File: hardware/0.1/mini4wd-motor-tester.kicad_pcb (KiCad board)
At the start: 2 copper layers, 108 x 48 mm, 104 parts, among them J1 USB_C_Receptacle_USB2.0_16P, J2 JST SH, J3 JST SH, J4 JST XH, M1 Motor_DC, Q2 AO3401A, Q3 2N7002, SW1 RA, SW2 RA, SW3 EC11, U1 TLV62130, U10 GP2S700HCP, U2 USBLC6-2SC6, U3 RT9080-33GJ5, U4 MCP4725, U5 ESP32-S3-WROOM-1, U6 INA219AxDCN, U7 DRV8837, U8 GP2S700HCP, U9 TMP1075DSG

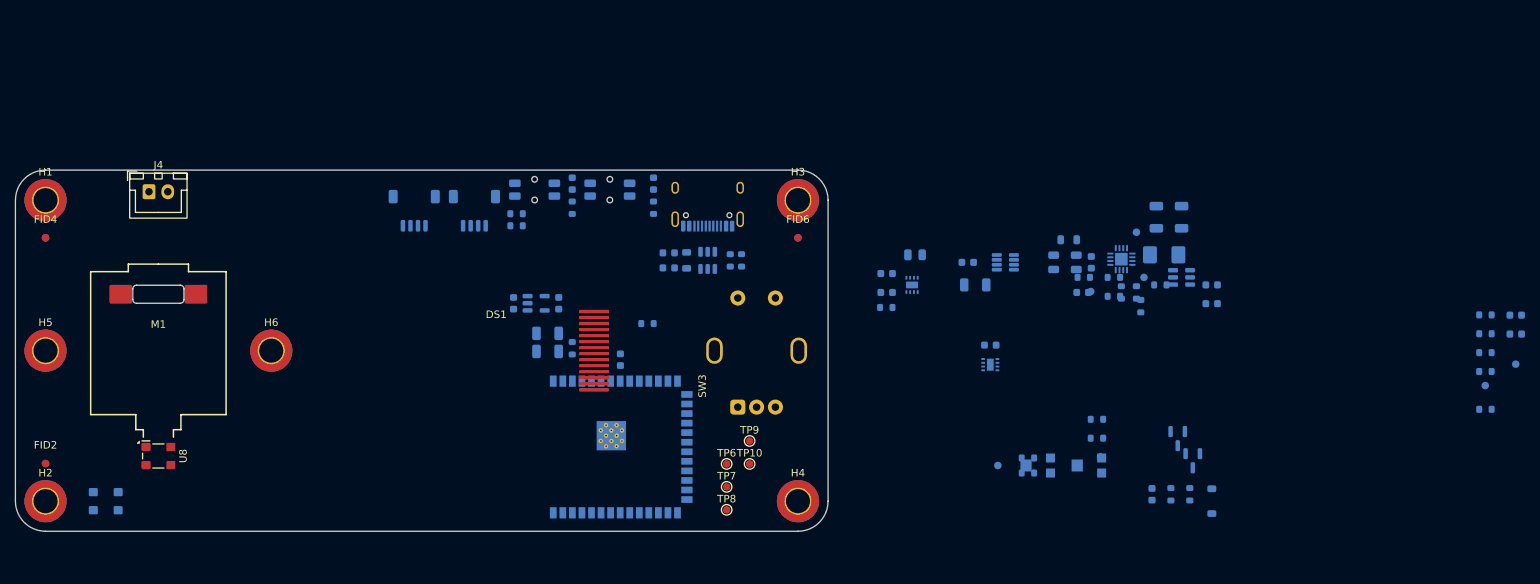
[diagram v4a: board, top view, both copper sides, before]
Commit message: rough placement of all parts on smaller board
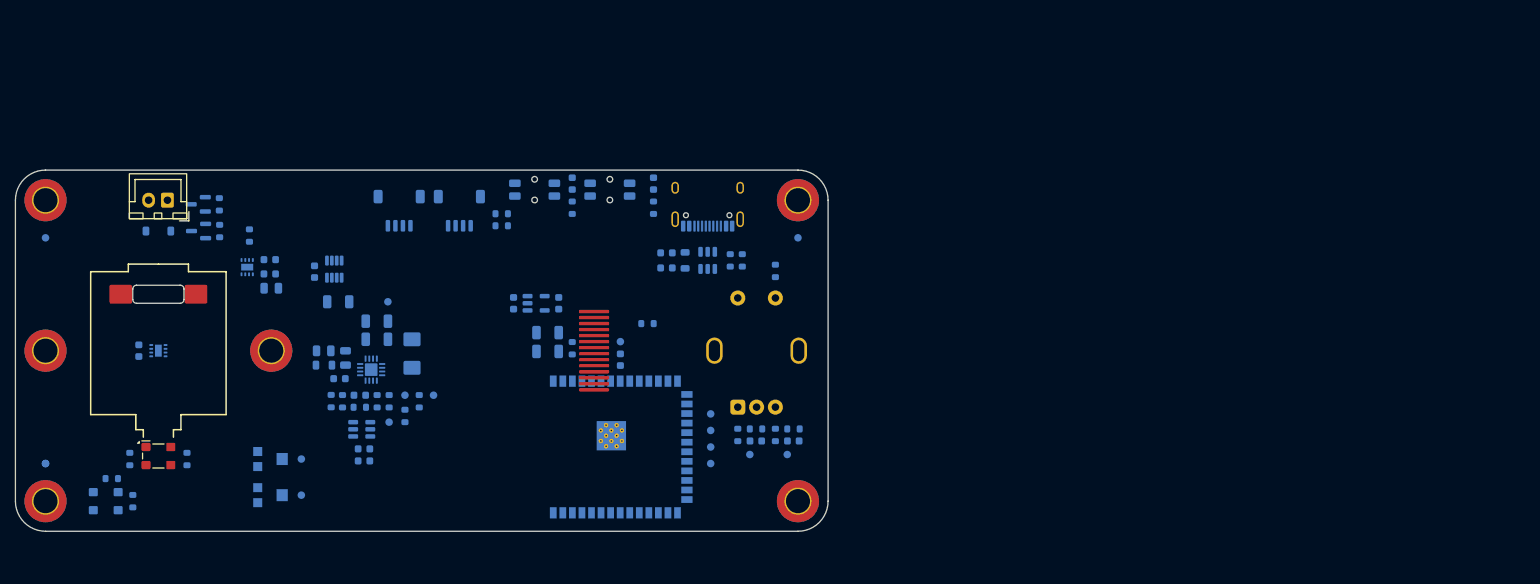
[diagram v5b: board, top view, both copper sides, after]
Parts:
- removed C24: 100n, Capacitor_SMD:C_0603_1608Metric
- removed FID4, FID6: Fiducial, Fiducial:Fiducial_1mm_Mask3mm
- added TP13: TP, TestPoint:TestPoint_Pad_D1.0mm, B.Cu at (121.6, 105.9)
- C12: value 100n -> 1u
- FID2, TP10, TP6, TP7, TP8, TP9: moved to B.Cu
- moved D3 144.5 mm to (85.0, 84.1), turned to 180 degrees
- moved Q2 135.6 mm to (90.3, 84.1), turned to 180 degrees
- moved Q3 133.8 mm to (90.3, 80.5), turned to 180 degrees
- moved R28 133.6 mm to (93.1, 84.1)
- moved R27 132.2 mm to (93.1, 80.5)
- moved R25 131.2 mm to (78.8, 117.0)
- moved R26 128.4 mm to (81.6, 120.0), turned to -90 degrees
- moved R22 119.4 mm to (81.2, 114.4), turned to -90 degrees
- moved C11 114.7 mm to (112.3, 113.0), turned to 180 degrees
- moved C12 114.6 mm to (112.3, 114.7)
- moved C22 113.2 mm to (82.4, 100.0), turned to 90 degrees
- moved R17 111.8 mm to (88.8, 114.4), turned to -90 degrees
- moved U4 110.8 mm to (112.0, 110.5), turned to 180 degrees
- moved U9 110.6 mm to (85.0, 100.0)
- moved RV2 108.6 mm to (100.0, 119.2), turned to 0 degrees
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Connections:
- C12 pad 1: +3V3 -> GND
- C12 pad 2: GND -> +3V3
- R6 pad 1: +VMOT -> +3V3

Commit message: I think the final form has been reached?
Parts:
- removed FID5: Fiducial, Fiducial:Fiducial_1mm_Mask3mm
- added G1: ~, josh-logos:josh-details, B.Cu at (103.0, 82.2)
- added kibuzzard-697A0689: G***, kibuzzard-697A0689, F.Cu at (125.0, 121.0)
- moved FID2 30.0 mm to (70.0, 85.0)
- moved R28 17.0 mm to (76.2, 84.1), turned to 90 degrees
- moved Q3 14.9 mm to (77.3, 87.8)
- moved R27 14.9 mm to (80.1, 87.8)
- moved Q2 11.4 mm to (79.0, 84.1), turned to 0 degrees
- moved H3 8.00 mm to (162.0, 80.0)
- moved H4 8.00 mm to (162.0, 120.0)
- moved FID1 7.99 mm to (162.0, 85.0)
- moved U5 7.65 mm to (135.1, 111.9)
- moved R24 7.65 mm to (142.4, 95.5)
- moved TP10 7.60 mm to (150.8, 108.4)
- moved TP6 7.60 mm to (150.8, 110.6)
- moved TP7 7.60 mm to (150.8, 115.0)
- moved TP9 7.60 mm to (150.8, 112.8)
- moved SW3 7.50 mm to (154.5, 107.5)
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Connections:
- J4 pad 1: Net-(D3-K) -> GND
- J4 pad 2: GND -> Net-(D3-K)
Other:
- board size 108 x 48 mm -> 100 x 48 mm
- board text added: "+"
- board text added: "-"
- board text added: "BOOT"
- board text added: "I2C"
- board text added: "MINI4WD MOTOR TESTER REVISION 1.0"
- board text added: "PWR"
- board text added: "RESET"
- board text added: "STAT"
- board text added: "UART"

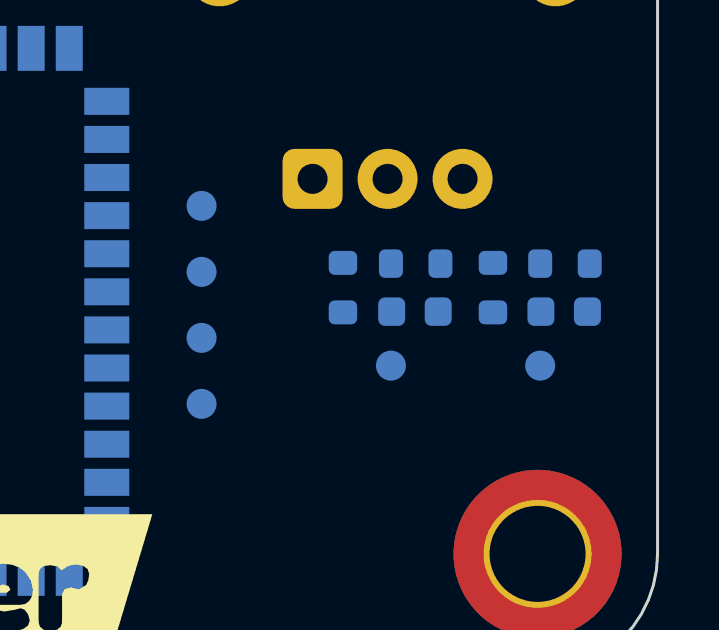
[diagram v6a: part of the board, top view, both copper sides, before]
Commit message: move encoder passives in from the edge
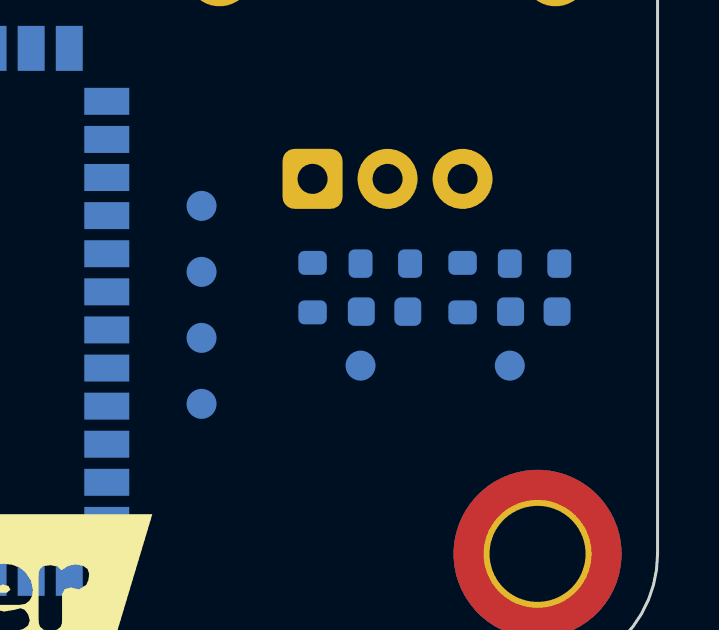
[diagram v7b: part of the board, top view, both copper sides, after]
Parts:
- moved TP4 1.01 mm to (156.1, 113.7)
- moved TP5 1.01 mm to (161.1, 113.7)
- moved C20 1.01 mm to (156.9, 111.9)
- moved C21 1.01 mm to (161.9, 111.9)
- moved R18 1.01 mm to (154.5, 111.1)
- moved R19 1.01 mm to (156.9, 110.3)
- moved R20 1.01 mm to (159.5, 111.1)
- moved R21 1.01 mm to (161.9, 110.3)
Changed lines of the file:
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@@
 	(footprint "Capacitor_SMD:C_0603_1608Metric"
 		(layer "B.Cu")
-		(at 162.8875 111.925)
+		(at 161.875 111.925)
 		(descr "Capacitor SMD 0603 (1608 Metric), square (rectangular) end terminal, IPC-7351 nominal, (Body size source: IPC-SM-782 page 76, https://www.pcb-3d.com/wordpress/wp-content/uploads/ipc-sm-782a_amendment_1_and_2.pdf), generated with kicad-footprint-generator")
 		(tags "capacitor")
@@
 	(footprint "Resistor_SMD:R_0603_1608Metric"
 		(layer "B.Cu")
-		(at 162.9125 110.325 180)
+		(at 161.9 110.325 180)
 		(descr "Resistor SMD 0603 (1608 Metric), square (rectangular) end terminal, IPC-7351 nominal, (Body size source: IPC-SM-782 page 72, https://www.pcb-3d.com/wordpress/wp-content/uploads/ipc-sm-782a_amendment_1_and_2.pdf), generated with kicad-footprint-generator")
 		(tags "resistor")
@@
 	(footprint "TestPoint:TestPoint_Pad_D1.0mm"
 		(layer "B.Cu")
-		(at 157.1125 113.725 180)
+		(at 156.1 113.725 180)
 		(descr "SMD pad as test Point, diameter 1.0mm")
 		(tags "test point SMD pad")
@@
 	(footprint "Resistor_SMD:R_0603_1608Metric"
 		(layer "B.Cu")
-		(at 155.5125 111.125 90)
+		(at 154.5 111.125 90)
 		(descr "Resistor SMD 0603 (1608 Metric), square (rectangular) end terminal, IPC-7351 nominal, (Body size source: IPC-SM-782 page 72, https://www.pcb-3d.com/wordpress/wp-content/uploads/ipc-sm-782a_amendment_1_and_2.pdf), generated with kicad-footprint-generator")
 		(tags "resistor")
@@
 	(footprint "Capacitor_SMD:C_0603_1608Metric"
 		(layer "B.Cu")
-		(at 157.9125 111.925)
+		(at 156.9 111.925)
 		(descr "Capacitor SMD 0603 (1608 Metric), square (rectangular) end terminal, IPC-7351 nominal, (Body size source: IPC-SM-782 page 76, https://www.pcb-3d.com/wordpress/wp-content/uploads/ipc-sm-782a_amendment_1_and_2.pdf), generated with kicad-footprint-generator")
 		(tags "capacitor")
@@
 	(footprint "Resistor_SMD:R_0603_1608Metric"
 		(layer "B.Cu")
-		(at 160.5125 111.125 90)
+		(at 159.5 111.125 90)
 		(descr "Resistor SMD 0603 (1608 Metric), square (rectangular) end terminal, IPC-7351 nominal, (Body size source: IPC-SM-782 page 72, https://www.pcb-3d.com/wordpress/wp-content/uploads/ipc-sm-782a_amendment_1_and_2.pdf), generated with kicad-footprint-generator")
 		(tags "resistor")
@@
 	(footprint "TestPoint:TestPoint_Pad_D1.0mm"
 		(layer "B.Cu")
-		(at 162.0875 113.725 180)
+		(at 161.075 113.725 180)
 		(descr "SMD pad as test Point, diameter 1.0mm")
 		(tags "test point SMD pad")
@@
 	(footprint "Resistor_SMD:R_0603_1608Metric"
 		(layer "B.Cu")
-		(at 157.9375 110.325 180)
+		(at 156.925 110.325 180)
 		(descr "Resistor SMD 0603 (1608 Metric), square (rectangular) end terminal, IPC-7351 nominal, (Body size source: IPC-SM-782 page 72, https://www.pcb-3d.com/wordpress/wp-content/uploads/ipc-sm-782a_amendment_1_and_2.pdf), generated with kicad-footprint-generator")
 		(tags "resistor")

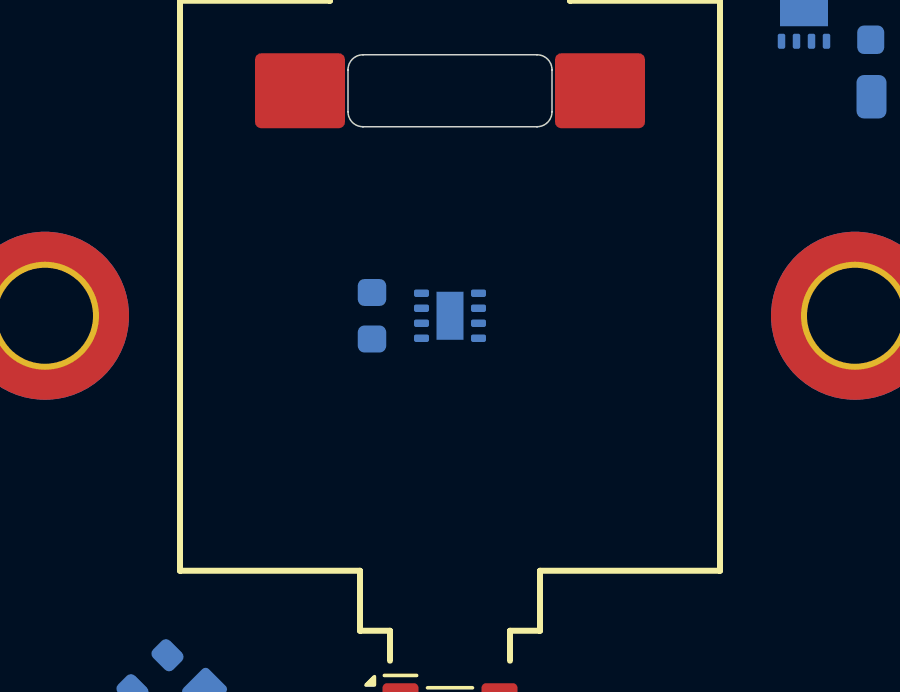
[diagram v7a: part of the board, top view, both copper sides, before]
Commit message: cutouts under the motor
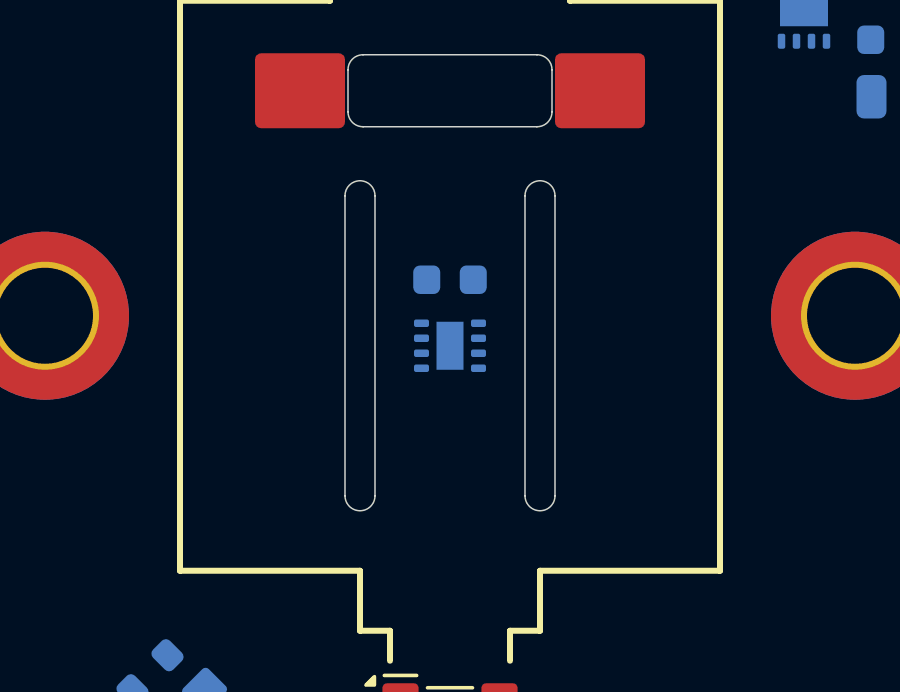
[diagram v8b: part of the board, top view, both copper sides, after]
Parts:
- moved C22 2.86 mm to (84.0, 98.8), turned to 180 degrees
- moved U9 1.00 mm to (84.0, 101.0)
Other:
- outline, holes or cut-outs redrawn
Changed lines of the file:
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@@
 		(tags "refective opto couple photo coupler")
 		(property "Reference" "U8"
-			(at 0 0 -0)
+			(at 0 0 0)
 			(layer "B.SilkS")
 			(effects
@@
 				(font
 					(size 0.001 0.001)
+					(thickness 0.15)
 				)
 			)
@@
 				(font
 					(size 0.001 0.001)
+					(thickness 0.15)
 				)
 			)
@@
 	(footprint "Package_SON:WSON-8-1EP_2x2mm_P0.5mm_EP0.9x1.6mm"
 		(layer "B.Cu")
-		(at 84 100 180)
+		(at 84 101 180)
 		(descr "8-Lead Plastic WSON, 2x2mm Body, 0.5mm Pitch, WSON-8, http://www.ti.com/lit/ds/symlink/lm27761.pdf")
 		(tags "WSON 8 1EP")
 		(property "Reference" "U9"
-			(at 0 2 0)
+			(at 0 -2.1 0)
 			(layer "B.SilkS")
 			(effects
@@
 	(footprint "Capacitor_SMD:C_0603_1608Metric"
 		(layer "B.Cu")
-		(at 81.4 100 90)
+		(at 84 98.8 180)
 		(descr "Capacitor SMD 0603 (1608 Metric), square (rectangular) end terminal, IPC-7351 nominal, (Body size source: IPC-SM-782 page 76, https://www.pcb-3d.com/wordpress/wp-content/uploads/ipc-sm-782a_amendment_1_and_2.pdf), generated with kicad-footprint-generator")
 		(tags "capacitor")
 		(property "Reference" "C22"
-			(at 0 1.43 90)
+			(at 0 1.43 0)
 			(layer "B.SilkS")
 			(hide yes)
@@
 		)
 		(property "Value" "100n"
-			(at 0 -1.43 90)
+			(at 0 -1.43 0)
 			(layer "B.Fab")
 			(effects
@@
 		)
 		(property "Datasheet" "~"
-			(at 0 0 90)
+			(at 0 0 0)
 			(layer "B.Fab")
 			(hide yes)
@@
 		)
 		(property "Description" ""
-			(at 0 0 90)
+			(at 0 0 0)
 			(layer "B.Fab")
 			(hide yes)
@@
 		)
 		(property "LCSC" "C14663"
-			(at 0 0 270)
+			(at 0 0 0)
 			(unlocked yes)
 			(layer "B.Fab")
@@
 		)
 		(property "Manufacturer" "Samsung Electro-Mechanics"
-			(at 0 0 270)
+			(at 0 0 0)
 			(unlocked yes)
 			(layer "B.Fab")
@@
 		)
 		(property "MPN " "CC0603KRX7R9BB104"
-			(at 0 0 270)
+			(at 0 0 0)
 			(unlocked yes)
 			(layer "B.Fab")
@@
 		)
 		(property "JLCSMT" ""
-			(at 0 0 90)
+			(at 0 0 180)
 			(unlocked yes)
 			(layer "B.Fab")
@@
 		(attr smd)
 		(fp_line
-			(start -0.14058 -0.51)
-			(end 0.14058 -0.51)
+			(start -0.14058 0.51)
+			(end 0.14058 0.51)
 			(stroke
 				(width 0.12)
@@
 		)
 		(fp_line
-			(start -0.14058 0.51)
-			(end 0.14058 0.51)
+			(start -0.14058 -0.51)
+			(end 0.14058 -0.51)
 			(stroke
 				(width 0.12)
@@
 		)
 		(fp_text user "${REFERENCE}"
-			(at 0 0 90)
+			(at 0 0 0)
 			(layer "B.Fab")
 			(effects
@@
 		)
 		(pad "1" smd roundrect
-			(at -0.775 0 90)
+			(at -0.775 0 180)
 			(size 0.9 0.95)
 			(layers "B.Cu" "B.Mask" "B.Paste")
@@
 		)
 		(pad "2" smd roundrect
-			(at 0.775 0 90)
+			(at 0.775 0 180)
 			(size 0.9 0.95)
 			(layers "B.Cu" "B.Mask" "B.Paste")
@@
 		)
 	)
+	(gr_rect
+		(start 78 94.5)
+		(end 90 107.5)
+		(stroke
+			(width 0.1)
+			(type solid)
+		)
+		(fill yes)
+		(layer "F.Mask")
+	)
+	(gr_arc
+		(start 80.5 96)
+		(mid 81 95.5)
+		(end 81.5 96)
+		(stroke
+			(width 0.05)
+			(type default)
+		)
+		(layer "Edge.Cuts")
+	)
 	(gr_line
 		(start 166 80)
@@
 	)
 	(gr_line
+		(start 81.5 96)
+		(end 81.5 106)
+		(stroke
+			(width 0.05)
+			(type default)
+		)
+		(layer "Edge.Cuts")
+	)
+	(gr_line
 		(start 66 80)
 		(end 66 120)
@@
 	)
 	(gr_arc
+		(start 86.5 96)
+		(mid 87 95.5)
+		(end 87.5 96)
+		(stroke
+			(width 0.05)
+			(type default)
+		)
+		(layer "Edge.Cuts")
+	)
+	(gr_line
+		(start 87.5 96)
+		(end 87.5 106)
+		(stroke
+			(width 0.05)
+			(type default)
+		)
+		(layer "Edge.Cuts")
+	)
+	(gr_arc
 		(start 166 120)
 		(mid 164.828427 122.828427)
@@
 			(type default)
 		)
+		(layer "Edge.Cuts")
+	)
+	(gr_arc
+		(start 81.5 106)
+		(mid 81 106.5)
+		(end 80.5 106)
+		(stroke
+			(width 0.05)
+			(type default)
+		)
+		(layer "Edge.Cuts")
+	)
+	(gr_line
+		(start 86.5 106)
+		(end 86.5 96)
+		(stroke
+			(width 0.05)
+			(type default)
+		)
+		(layer "Edge.Cuts")
+	)
+	(gr_line
+		(start 80.5 106)
+		(end 80.5 96)
+		(stroke
+			(width 0.05)
+			(type default)
+		)
+		(layer "Edge.Cuts")
+	)
+	(gr_arc
+		(start 87.5 106)
+		(mid 87 106.5)
+		(end 86.5 106)
+		(stroke
+			(width 0.05)
+			(type default)
+		)
